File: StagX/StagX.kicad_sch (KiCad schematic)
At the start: 3 parts

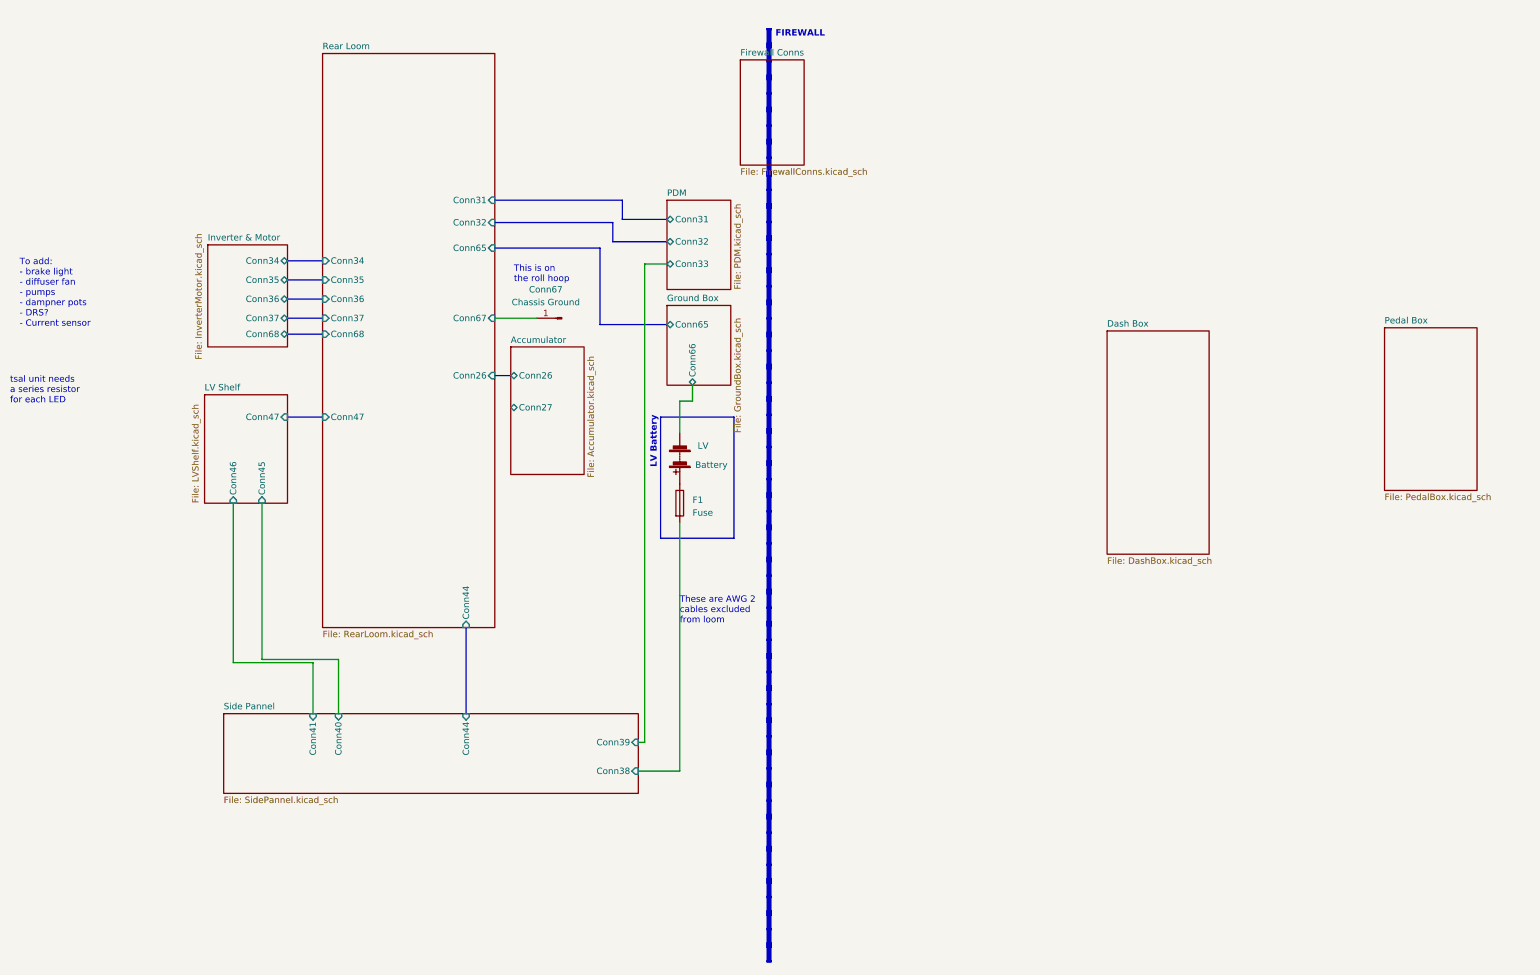
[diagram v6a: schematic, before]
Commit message: feat(RearLoom): PWR and GND complete. progress on top-level
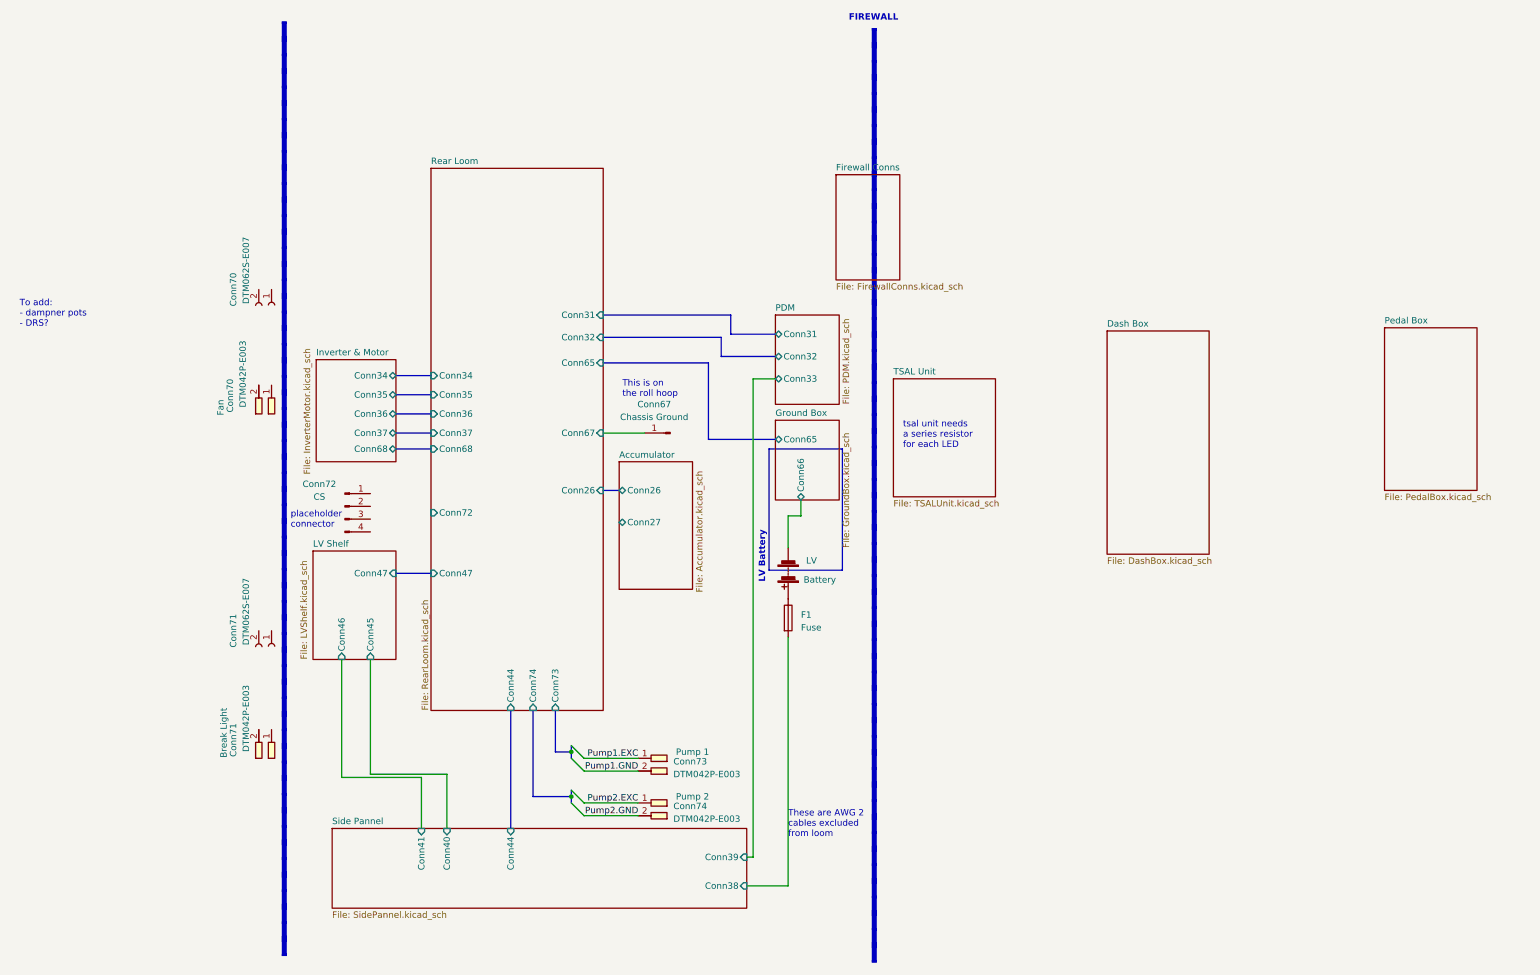
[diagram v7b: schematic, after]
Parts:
- added Conn70, Conn71, Conn73, Conn74: Deutsch_DTM_2P_Pin, symbol Connectors_SUFST:Deutsch_DTM_2P_Pin
- added Conn70, Conn71: Deutsch_DTM_2S_Pin, symbol Connectors_SUFST:Deutsch_DTM_2S_Pin
- added Conn72: CS, symbol Connector:Conn_01x04_Pin
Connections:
- new net Pump1.EXC: Conn73.1
- new net Pump1.GND: Conn73.2
- new net Pump2.EXC: Conn74.1
- new net Pump2.GND: Conn74.2
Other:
- added sheet TSAL Unit (TSALUnit.kicad_sch)
- sheet Rear Loom ports: added Conn72, Conn73, Conn74; removed none
- note added: "To add: - dampner pots - DRS?"
- note added: "placeholder connector"
- note removed: "To add: - brake light - diffuser fan - pumps - dampner pots - DRS? - Current sensor"
- moved on the sheet: Conn67, F1, LV

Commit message: feat(RearLoom): Rear Loom Completed
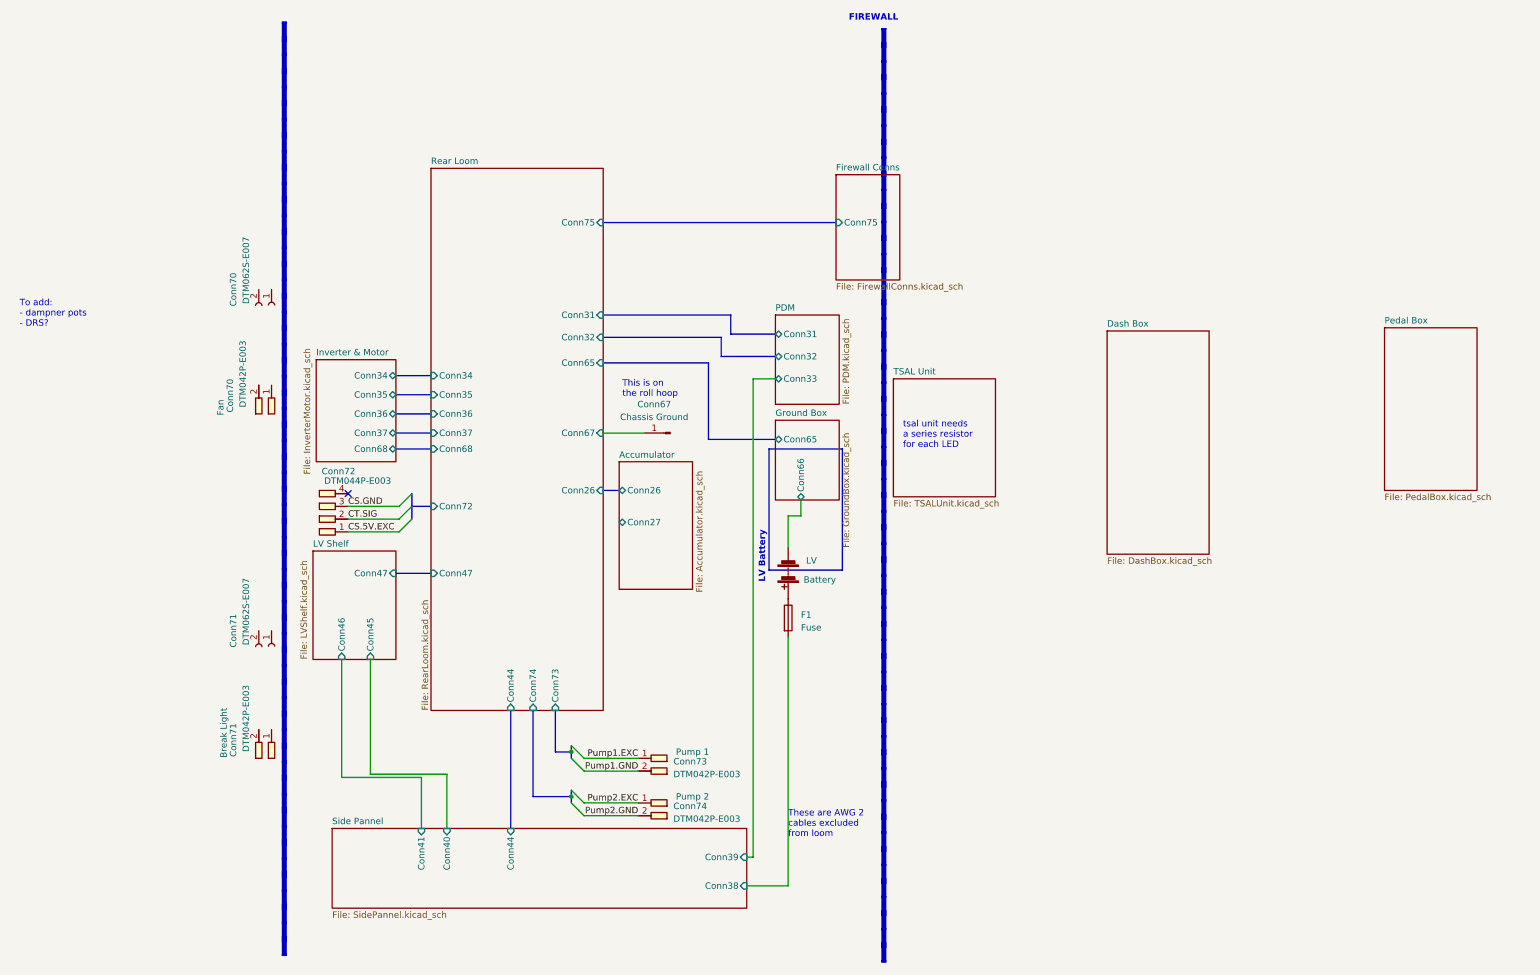
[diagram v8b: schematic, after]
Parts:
- removed Conn72: CS, symbol Connector:Conn_01x04_Pin
- added Conn72: Current Sensor, symbol Connectors_SUFST:Current Sensor
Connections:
- new net CS.5V.EXC: Conn72.1
- new net CS.GND: Conn72.3
- new net CT.SIG: Conn72.2
- no-connect marks 0 -> 1
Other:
- sheet Firewall Conns ports: added Conn75; removed none
- sheet Rear Loom ports: added Conn75; removed none
- note removed: "placeholder connector"
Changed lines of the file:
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@@
   (junction (at 90.805 156.845) (diameter 0) (color 0 0 0 0)
   )
+  (no_connect (at 46.355 105.41))
+  (bus_entry (at 56.515 107.95) (size 2.54 -2.54)
+    (stroke (width 0) (type default))
+  )
   (bus_entry (at 90.805 167.005) (size 2.54 2.54)
     (stroke (width 0) (type default))
@@
     (stroke (width 0) (type default))
   )
+  (bus_entry (at 56.515 110.49) (size 2.54 -2.54)
+    (stroke (width 0) (type default))
+  )
+  (bus_entry (at 56.515 113.03) (size 2.54 -2.54)
+    (stroke (width 0) (type default))
+  )
   (bus_entry (at 90.805 164.465) (size 2.54 2.54)
     (stroke (width 0) (type default))
@@
     (stroke (width 0) (type default))
   )
+  (wire (pts (xy 46.355 110.49) (xy 56.515 110.49))
+    (stroke (width 0) (type default))
+  )
   (bus (pts (xy 55.88 81.915) (xy 62.865 81.915))
     (stroke (width 0) (type default))
   )
+  (bus (pts (xy 59.055 107.95) (xy 59.055 110.49))
+    (stroke (width 0) (type default))
+  )
   (bus (pts (xy 55.88 121.285) (xy 62.865 121.285))
     (stroke (width 0) (type default))
@@
     (stroke (width 0) (type default))
   )
+  (bus (pts (xy 97.155 51.435) (xy 143.51 51.435))
+    (stroke (width 0) (type default))
+  )
   (bus (pts (xy 122.555 69.85) (xy 122.555 73.66))
     (stroke (width 0) (type default))
@@
     (stroke (width 0) (type default))
   )
+  (bus (pts (xy 59.055 107.95) (xy 62.865 107.95))
+    (stroke (width 0) (type default))
+  )
   (bus (pts (xy 90.805 155.575) (xy 90.805 156.845))
     (stroke (width 0) (type default))
@@
     (stroke (width 0) (type default))
   )
+  (wire (pts (xy 46.355 107.95) (xy 56.515 107.95))
+    (stroke (width 0) (type default))
+  )
   (wire (pts (xy 60.96 161.925) (xy 45.085 161.925))
     (stroke (width 0) (type default))
@@
     (stroke (width 0) (type default))
   )
+  (wire (pts (xy 46.355 113.03) (xy 56.515 113.03))
+    (stroke (width 0) (type default))
+  )
   (bus (pts (xy 90.805 156.845) (xy 90.805 158.115))
     (stroke (width 0) (type default))
@@
     (stroke (width 0) (type default))
   )
+  (bus (pts (xy 59.055 105.41) (xy 59.055 107.95))
+    (stroke (width 0) (type default))
+  )
   (wire (pts (xy 127 82.55) (xy 131.445 82.55))
     (stroke (width 0) (type default))
@@
     (stroke (width 0) (type default))
   )
-  (rectangle (start 151.13 12.7) (end 151.13 198.755)
+  (rectangle (start 153.035 12.7) (end 153.035 198.755)
     (stroke (width 1) (type dot) (color 255 0 0 1))
     (fill (type none))
@@
     (effects (font (size 1.27 1.27) (thickness 0.254) bold (color 255 0 0 1)) (justify left bottom))
   )
-  (text "placeholder\nconnector" (at 34.925 112.395 0)
-    (effects (font (size 1.27 1.27)) (justify left bottom))
-  )
   (text "tsal unit needs \na series resistor\nfor each LED" (at 156.845 96.52 0)
     (effects (font (size 1.27 1.27)) (justify left bottom))
@@
     (effects (font (size 1.27 1.27)) (justify right bottom))
   )
+  (label "CS.5V.EXC" (at 46.355 113.03 0) (fields_autoplaced)
+    (effects (font (size 1.27 1.27)) (justify left bottom))
+  )
   (label "Pump2.GND" (at 104.14 169.545 180) (fields_autoplaced)
     (effects (font (size 1.27 1.27)) (justify right bottom))
@@
   (label "Pump1.GND" (at 104.14 160.655 180) (fields_autoplaced)
     (effects (font (size 1.27 1.27)) (justify right bottom))
+  )
+  (label "CS.GND" (at 46.355 107.95 0) (fields_autoplaced)
+    (effects (font (size 1.27 1.27)) (justify left bottom))
+  )
+  (label "CT.SIG" (at 46.355 110.49 0) (fields_autoplaced)
+    (effects (font (size 1.27 1.27)) (justify left bottom))
   )
   (label "Pump2.EXC" (at 104.14 167.005 180) (fields_autoplaced)
@@
     )
   )
-  (symbol (lib_id "Connector:Conn_01x04_Pin") (at 45.72 107.95 0) (unit 1)
-    (in_bom yes) (on_board yes) (dnp no)
-    (property "Reference" "Conn72" (at 40.64 103.505 0)
-      (effects (font (size 1.27 1.27)))
-    )
-    (property "Value" "CS" (at 40.64 106.045 0)
-      (effects (font (size 1.27 1.27)))
-    )
-    (property "Footprint" "" (at 45.72 107.95 0)
-      (effects (font (size 1.27 1.27)) hide)
-    )
-    (property "Datasheet" "~" (at 45.72 107.95 0)
-      (effects (font (size 1.27 1.27)) hide)
+  (symbol (lib_id "Connectors_SUFST:Current Sensor") (at 44.45 100.965 0) (unit 1)
+    (in_bom yes) (on_board yes) (dnp no)
+    (property "Reference" "Conn72" (at 44.45 100.965 0)
+      (effects (font (size 1.27 1.27)))
+    )
+    (property "Value" "Current Sensor" (at 44.45 100.965 0)
+      (effects (font (size 1.27 1.27)) hide)
+    )
+    (property "Footprint" "" (at 44.45 100.965 0)
+      (effects (font (size 1.27 1.27)) hide)
+    )
+    (property "Datasheet" "" (at 44.45 100.965 0)
+      (effects (font (size 1.27 1.27)) hide)
+    )
+    (property "P/N" "DTM044P-E003" (at 48.26 102.87 0)
+      (effects (font (size 1.27 1.27)))
     )
     (pin "1")
@@
       (effects (font (size 1.27 1.27)) (justify left))
     )
-    (pin "Conn72" input (at 62.865 109.22 180)
+    (pin "Conn72" input (at 62.865 107.95 180)
       (effects (font (size 1.27 1.27)) (justify left))
     )
@@
     (pin "Conn74" input (at 83.185 148.59 270)
       (effects (font (size 1.27 1.27)) (justify left))
+    )
+    (pin "Conn75" input (at 97.155 51.435 0)
+      (effects (font (size 1.27 1.27)) (justify right))
     )
     (instances
@@
       (effects (font (size 1.27 1.27)) (justify left top))
     )
-    (instances
+    (pin "Conn75" input (at 143.51 51.435 180)
+      (effects (font (size 1.27 1.27)) (justify left))
+    )
+    (instances
